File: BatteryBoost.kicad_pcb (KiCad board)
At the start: 2 copper layers, 80 x 40 mm, 4 parts, among them J1 Mounting Hole, J2 Mounting Hole, J3 Mounting Hole, J4 Mounting Hole

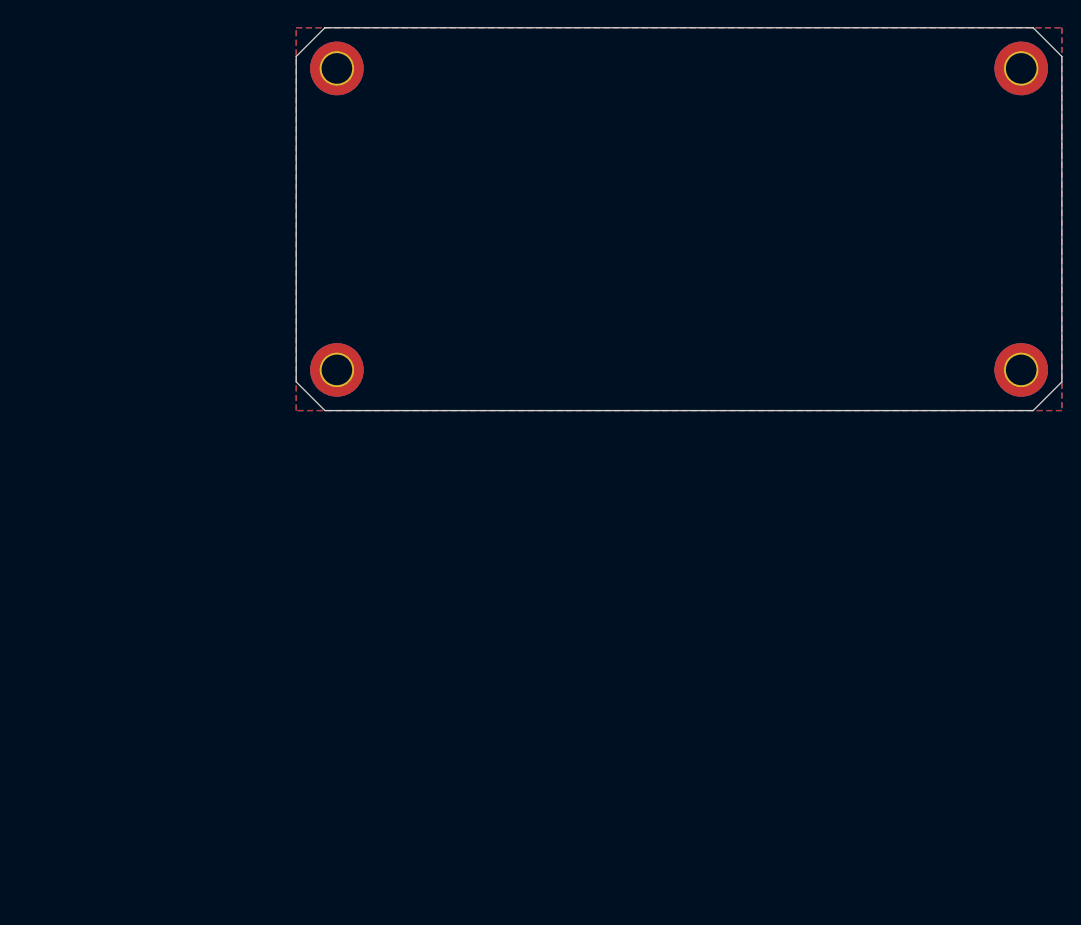
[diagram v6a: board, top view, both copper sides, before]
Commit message: Start placing footprints on board
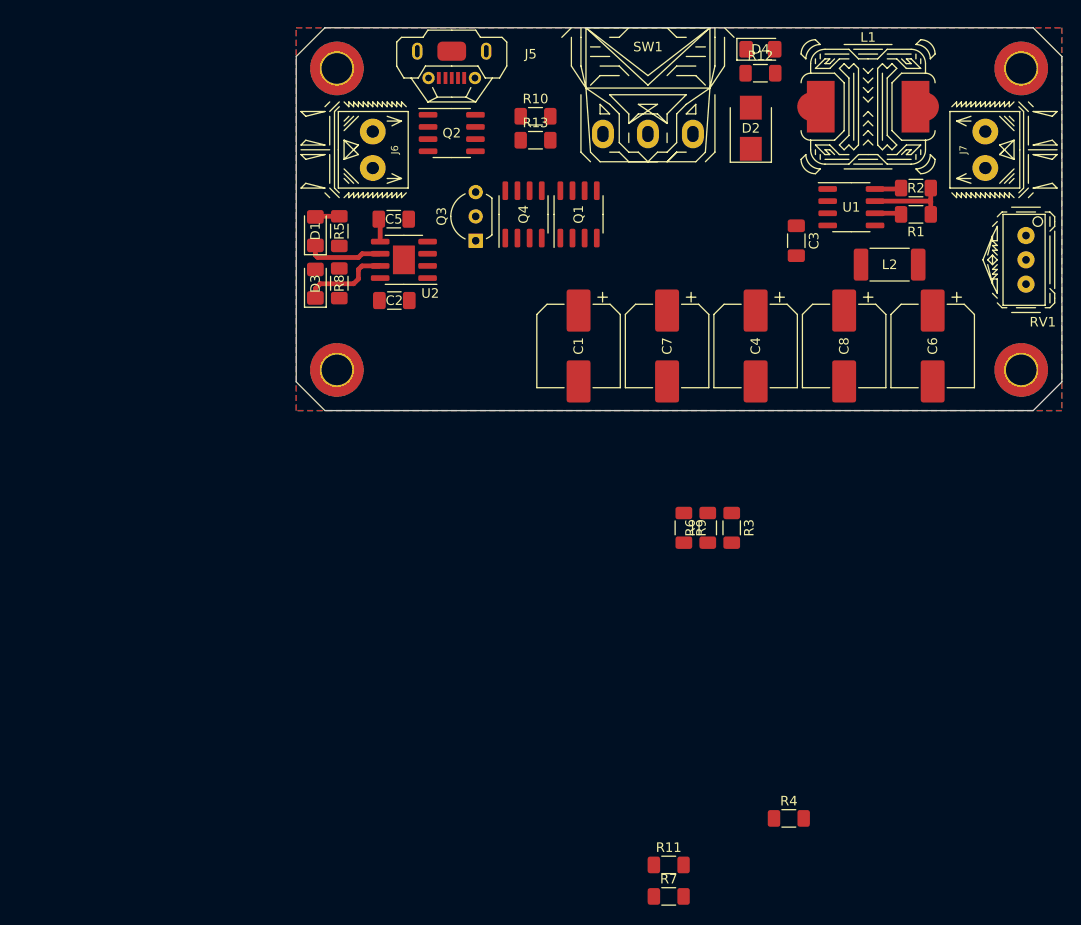
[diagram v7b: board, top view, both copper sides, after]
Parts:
- added C1: 100uF ±20% 50V, Capacitor_SMD:CP_Elec_8x10.5, F.Cu at (29.5, 33.2)
- added C2: 10uF ±10% 25V X5R, Capacitor_SMD:C_1206_3216Metric_Pad1.33x1.80mm_HandSolder, F.Cu at (10.2, 28.5)
- added C3: 1.5nF ±10% 50V X7R 1206, Capacitor_SMD:C_1206_3216Metric_Pad1.33x1.80mm_HandSolder, F.Cu at (52.2, 22.2)
- added C4: 100uF ±20% 50V, Capacitor_SMD:CP_Elec_8x10.5, F.Cu at (48.0, 33.2)
- added C5: 10uF ±10% 25V X5R, Capacitor_SMD:C_1206_3216Metric_Pad1.33x1.80mm_HandSolder, F.Cu at (10.2, 20.0)
- added C6: 100uF ±20% 50V, Capacitor_SMD:CP_Elec_8x10.5, F.Cu at (66.5, 33.2)
- added C7: 100uF ±20% 50V, Capacitor_SMD:CP_Elec_8x10.5, F.Cu at (38.8, 33.2)
- added C8: 100uF ±20% 50V (x3), Capacitor_SMD:CP_Elec_8x10.5, F.Cu at (57.2, 33.2)
- added D1: Blue LED, Diode_SMD:D_1206_3216Metric_Pad1.42x1.75mm_HandSolder, F.Cu at (2.00, 21.2)
- added D2: 40V 3A 500mV@3A, Diode_SMD:D_SMB, F.Cu at (47.5, 10.5)
- added D3: Red LED, Diode_SMD:D_1206_3216Metric_Pad1.42x1.75mm_HandSolder, F.Cu at (2.00, 26.7)
- added D4: Blue LED, Diode_SMD:D_1206_3216Metric_Pad1.42x1.75mm_HandSolder, F.Cu at (48.5, 2.25)
- added J5: USB_B_Micro, BatteryBoost:U-F-M5DD-Y-L, F.Cu at (16.2, 5.25)
- added J6: Battery, BatteryBoost:WJ124-3.81-2P, F.Cu at (8.00, 12.8)
- added J7: Output, BatteryBoost:WJ124-3.81-2P, F.Cu at (72.0, 12.8)
- added L1: 150uH ±20% 2.15A 280mΩ, BatteryBoost:Inductor_SLH_12x12x8_HandSolder, F.Cu at (59.8, 8.25)
- added L2: 1uH ±20% 3.29A 59mΩ, Inductor_SMD:L_2512_6332Metric_Pad1.52x3.35mm_HandSolder, F.Cu at (62.0, 24.8)
- added Q1: -40V 7.5A 2.5V @ 250uA 40mΩ @ 6A, Package_SO:SOIC-8_3.9x4.9mm_P1.27mm, F.Cu at (29.5, 19.5)
- added Q2: -40V 7.5A 2.5V @ 250uA 40mΩ @ 6A, Package_SO:SOIC-8_3.9x4.9mm_P1.27mm, F.Cu at (16.2, 11.0)
- added Q3: 60V 500mA 3V @ 1mA, Package_TO_SOT_THT:TO-92L_Inline_Wide, F.Cu at (18.8, 22.2)
- added Q4: -40V 7.5A 2.5V @ 250uA 40mΩ @ 6A, Package_SO:SOIC-8_3.9x4.9mm_P1.27mm, F.Cu at (23.8, 19.5)
- added R1: 0.3R, Resistor_SMD:R_1206_3216Metric_Pad1.30x1.75mm_HandSolder, F.Cu at (64.8, 19.5)
- added R10: 10k, Resistor_SMD:R_1206_3216Metric_Pad1.30x1.75mm_HandSolder, F.Cu at (25.0, 9.25)
- added R11: 1.2kΩ ±1% 0.25W, Resistor_SMD:R_1206_3216Metric_Pad1.30x1.75mm_HandSolder, F.Cu at (38.9, 87.5)
- added R12: 10k, Resistor_SMD:R_1206_3216Metric_Pad1.30x1.75mm_HandSolder, F.Cu at (48.5, 4.75)
- added R13: 10k, Resistor_SMD:R_1206_3216Metric_Pad1.30x1.75mm_HandSolder, F.Cu at (25.0, 11.8)
- added R2: 180R, Resistor_SMD:R_1206_3216Metric_Pad1.30x1.75mm_HandSolder, F.Cu at (64.8, 16.8)
- added R3: 499k 0.25W 1%, Resistor_SMD:R_1206_3216Metric_Pad1.30x1.75mm_HandSolder, F.Cu at (45.5, 52.2)
- added R4: 16k, Resistor_SMD:R_1206_3216Metric_Pad1.30x1.75mm_HandSolder, F.Cu at (51.5, 82.6)
- added R5: 10k, Resistor_SMD:R_1206_3216Metric_Pad1.30x1.75mm_HandSolder, F.Cu at (4.50, 21.2)
- added R6: 9.1k 1% 0.25W, Resistor_SMD:R_1206_3216Metric_Pad1.30x1.75mm_HandSolder, F.Cu at (43.0, 52.2)
- added R7: 0R, Resistor_SMD:R_1206_3216Metric_Pad1.30x1.75mm_HandSolder, F.Cu at (38.9, 90.8)
- added R8: 10k, Resistor_SMD:R_1206_3216Metric_Pad1.30x1.75mm_HandSolder, F.Cu at (4.50, 26.7)
- added R9: 47.5kΩ ±1% 0.25W, Resistor_SMD:R_1206_3216Metric_Pad1.30x1.75mm_HandSolder, F.Cu at (40.5, 52.2)
- added RV1: Variable Resistors 500kΩ ±10%, BatteryBoost:Potentiometer_3296W-1-504, F.Cu at (76.2, 24.2)
- added SW1: SW_SPDT, BatteryBoost:Switch_SS-12D06L5, F.Cu at (36.8, 0.00)
- added U1: SP34063AEN, Package_SO:SOIC-8_3.9x4.9mm_P1.27mm, F.Cu at (58.0, 18.8)
- added U2: TP4056, BatteryBoost:SOIC-8-1EP_3.9x4.9mm_P1.27mm_EP2.29x3mm, F.Cu at (11.2, 24.2)
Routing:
- net Net-(D3-Pad1): track 0.00 -> 9.32 mm
- net Net-(L1-Pad2): track 0.00 -> 8.61 mm
- net Net-(D1-Pad1): track 0.00 -> 8.05 mm
- net SMPS_Pwr: track 0.00 -> 2.77 mm
- net Net-(R2-Pad1): track 0.00 -> 2.76 mm
- net Net-(D1-Pad2): track 0.00 -> 2.44 mm
- net VBATT: track 0.00 -> 2.41 mm

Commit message: Add battery protection circuit
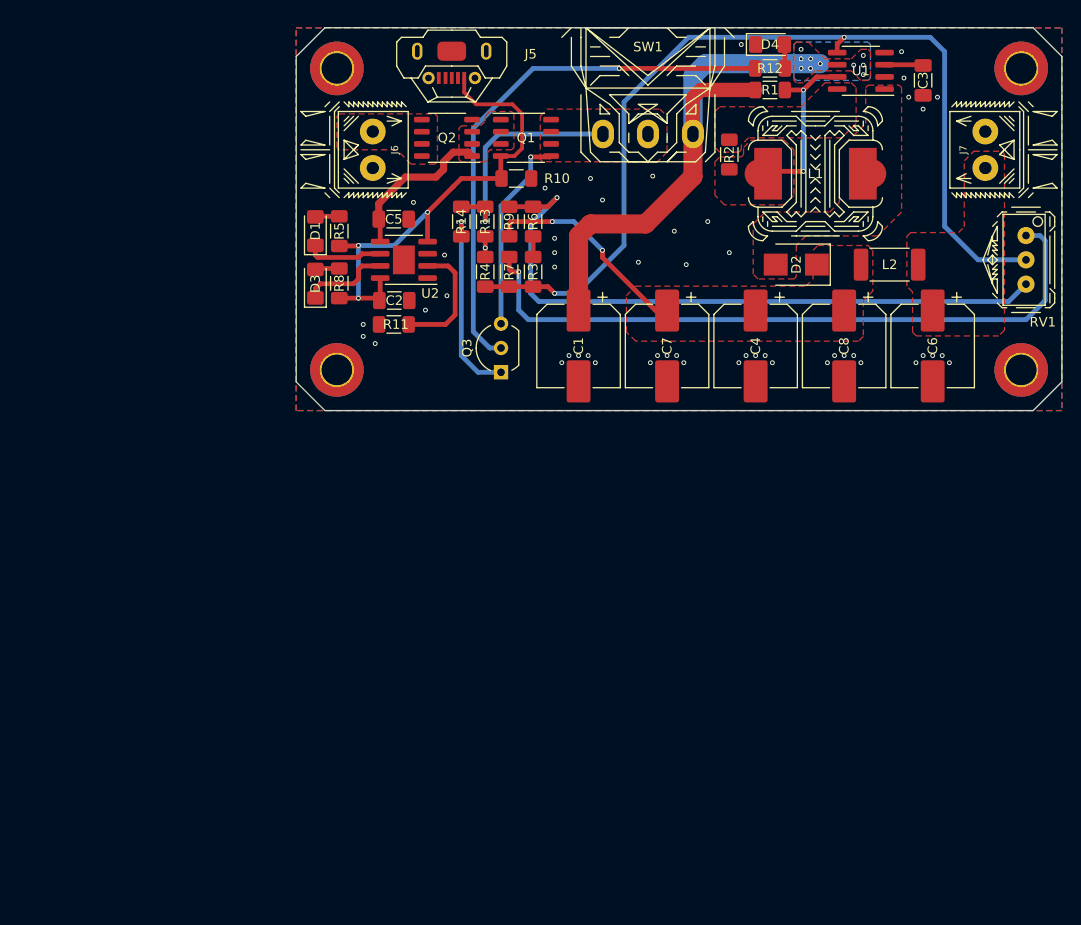
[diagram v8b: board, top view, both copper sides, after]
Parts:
- removed Q4: -40V 7.5A 2.5V @ 250uA 40mΩ @ 6A, Package_SO:SOIC-8_3.9x4.9mm_P1.27mm
- added R14: 10k, Resistor_SMD:R_1206_3216Metric_Pad1.30x1.75mm_HandSolder, F.Cu at (17.2, 20.2)
- Q1, Q2: footprint Package_SO:SOIC-8_3.9x4.9mm_P1.27mm -> BatteryBoost:SOP-8_3.9x4.9mm_P1.27mm
- Q3: value 60V 500mA 3V @ 1mA -> Q_PNP_BCE; footprint Package_TO_SOT_THT:TO-92L_Inline_Wide -> Package_TO_SOT_THT:TO-92_Inline_Wide
- moved R7 67.4 mm to (22.2, 25.5), turned to 270 degrees
- moved R4 65.3 mm to (19.8, 25.5), turned to 270 degrees
- moved R11 63.4 mm to (10.2, 31.0)
- moved R6 36.8 mm to (24.8, 20.2)
- moved R9 36.8 mm to (22.2, 20.2)
- moved R3 33.9 mm to (24.8, 25.5), turned to 90 degrees
- moved C3 21.4 mm to (65.5, 5.50)
- moved R1 20.0 mm to (49.5, 6.50)
- moved R2 19.8 mm to (45.2, 13.2), turned to 270 degrees
- moved D2 15.0 mm to (52.2, 24.8), turned to 180 degrees
- moved U1 14.3 mm to (59.0, 4.50), turned to 180 degrees
- moved Q3 14.0 mm to (21.4, 36.0)
- moved R13 9.99 mm to (19.8, 20.2), turned to 270 degrees
- moved Q1 9.71 mm to (24.0, 11.5), turned to 0 degrees
- moved L1 8.90 mm to (54.2, 15.2), turned to 270 degrees
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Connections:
- Q3 pad 2: +5V -> Net-(Q3-Pad2)
- Q3 pad 3: GND -> Net-(Q1-PadD)
- R12 pad 1: SMPS_Pwr -> Net-(Q3-Pad2)
- R13 pad 1: Net-(Q3-Pad1) -> Net-(R13-Pad1)
- R13 pad 2: +5V -> GND
- SW1 pad 1: SMPS_Pwr -> Net-(R13-Pad1)
- SW1 pad 2: SelectedSource -> Net-(Q1-PadD)
- SW1 pad 3: Net-(SW1-Pad3) -> SMPS_Pwr
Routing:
- net SMPS_VoltageSetting: track 0.00 -> 98.9 mm, vias 0 -> 2
- net Net-(R7-Pad1): track 0.00 -> 71.1 mm, vias 0 -> 1
- net Net-(R6-Pad2): track 0.00 -> 69.4 mm, vias 0 -> 1
- net Net-(Q3-Pad2): track 0.00 -> 56.9 mm, vias 0 -> 1
- net SMPS_Pwr: track 2.77 -> 57.3 mm, vias 0 -> 10
- net +5V: track 0.00 -> 52.1 mm, vias 0 -> 3
- net Net-(R13-Pad1): track 0.00 -> 24.7 mm, vias 0 -> 1
- net SMPS_Output: track 0.00 -> 23.6 mm, vias 0 -> 2
- net Net-(Q1-PadD): track 0.00 -> 20.9 mm, vias 0 -> 1
- net Net-(Q3-Pad1): track 0.00 -> 20.4 mm, vias 0 -> 1
- net VBATT: track 2.41 -> 16.6 mm
- net Net-(R11-Pad2): track 0.00 -> 12.8 mm
- net Net-(L1-Pad2): track 8.61 -> 18.3 mm, vias 0 -> 2
- net Net-(C3-Pad1): track 0.00 -> 4.06 mm
- net Net-(R2-Pad1): track 2.76 -> 0.00 mm
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- added copper zone on F.Cu, net /Vout
- added copper zone on F.Cu, net Net-(D2-Pad2)
- added copper zone on F.Cu, net Net-(J6-Pad1)
- added copper zone on F.Cu, net Net-(L1-Pad2)
- added copper zone on F.Cu, net Net-(Q1-PadD)
- added copper zone on F.Cu, net Net-(R2-Pad1)
- added copper zone on F.Cu, net SMPS_Output
- added copper zone on B.Cu, net SMPS_Pwr
- added copper zone on F.Cu, net SMPS_Pwr
- added copper zone on F.Cu, net VBATT
